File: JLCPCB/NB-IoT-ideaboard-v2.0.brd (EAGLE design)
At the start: 93 x 65 mm, 118 parts, among them Q1 32.768kHz, Q2 9013, Q3 9013, Q4 9013, Q5 9013, U1 STM32F103RBT6, U2 MCP73831T-2ACI/OT, U3 AP2112-3.3, U4 PAM2401, U5 MICROSIM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

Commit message: Readme.md
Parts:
- moved S4 0.20 mm to (30.7, 57.5)
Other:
- board text added: "BRAND"
- board text added: "Dialog IoT Device Information"
- board text added: "MAC"
- board text added: "MSISDN"
- board text added: "TYPE"
- board text added: "VERSION"

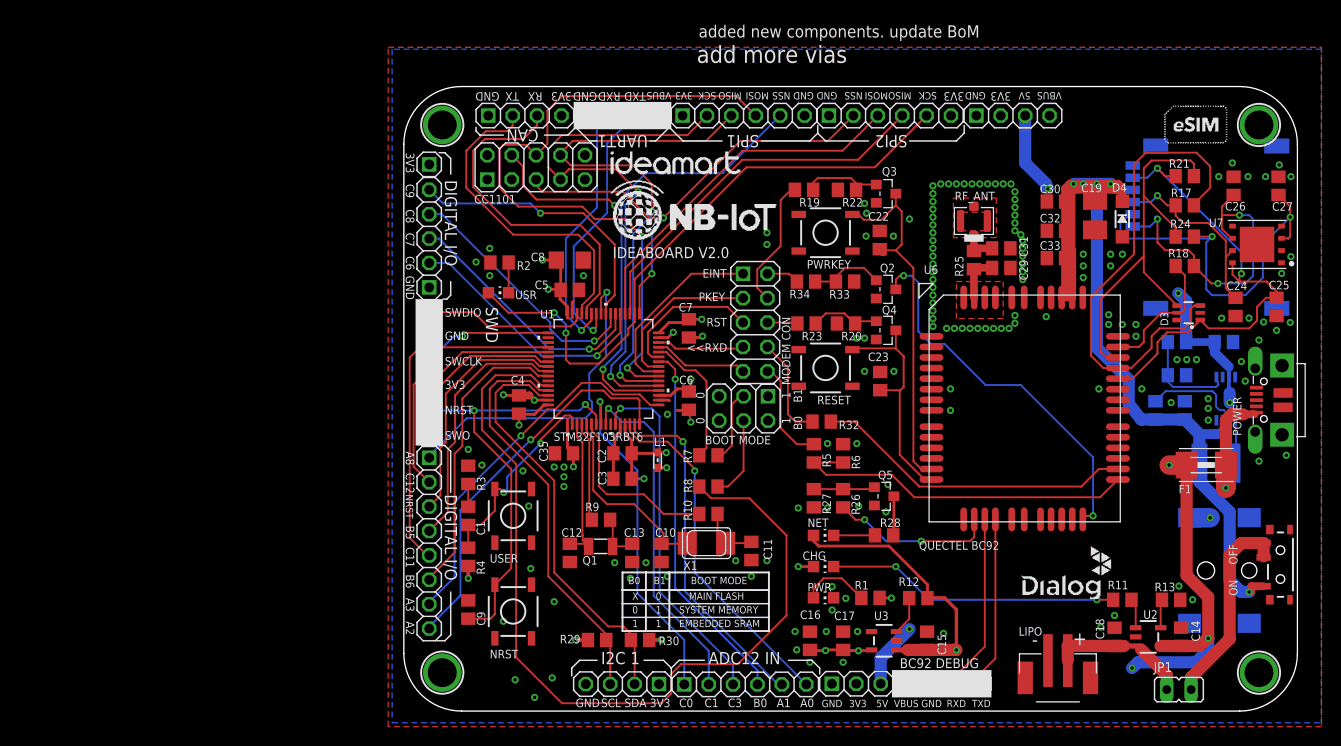
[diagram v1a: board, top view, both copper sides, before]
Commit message: Adds USB FS data lines for CDC Virtual Com port
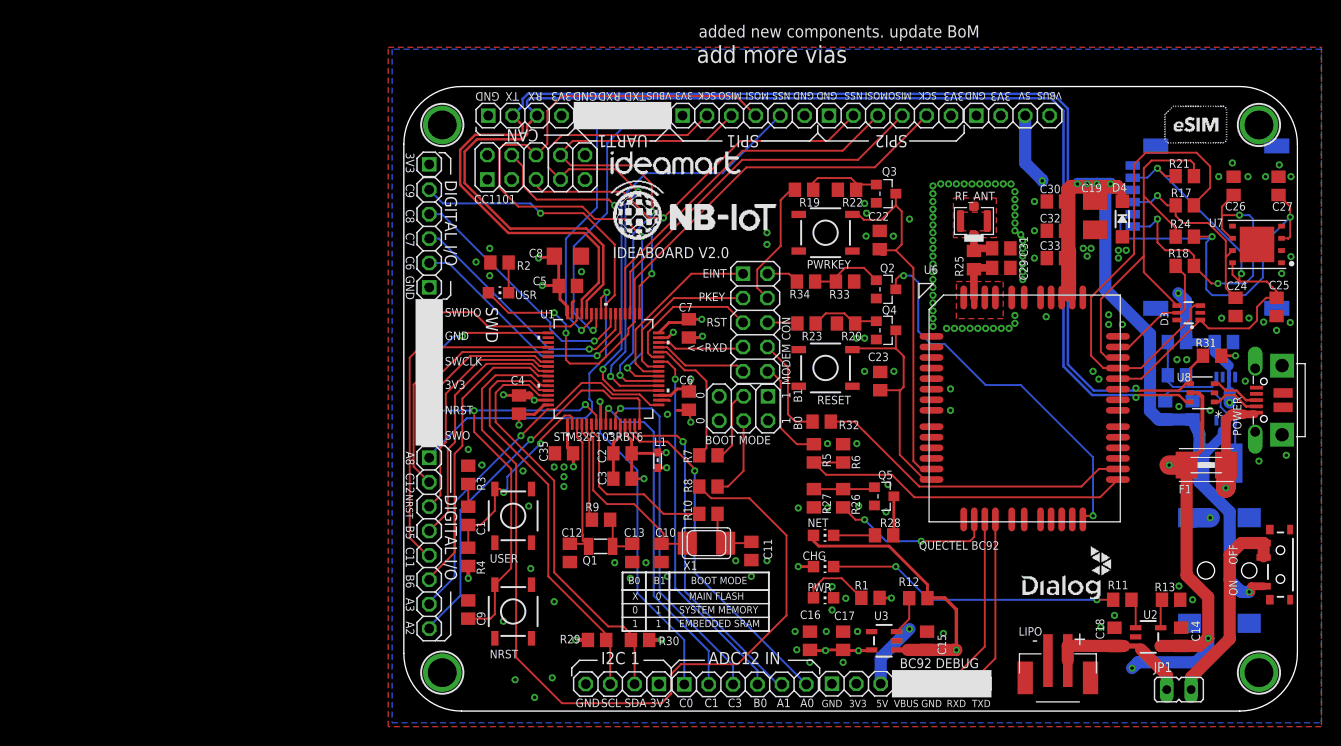
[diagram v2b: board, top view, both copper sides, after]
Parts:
- added R31: 1k5, rcl:R0805
- added U8: USBLC6-2SC6YSOT23-6L_STM-L, USBLC6:SOT23-6L_STM-L
- moved R14 1.02 mm to (98.6, 68.5)
- moved C20 0.81 mm to (101.4, 68.5)
- moved C5 0.45 mm to (36.4, 81.4)
- moved C8 0.45 mm to (36.4, 84.5)
- moved L2 0.20 mm to (104.0, 63.0)
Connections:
- removed net CAN_RX: CAN.3, U1.44
- removed net CAN_TX: CAN.2, U1.45
- removed net VSS: C2.1, C3.1, U1.12
- new net USB_CONN_D_N: POWER.D-, U8.1
- new net USB_CONN_D_P: POWER.D+, U8.3
- new net USB_D_N: CAN.3, U1.44, U8.6
- new net USB_D_P: CAN.2, R31.2, U1.45, U8.4
- net +3V3: now also R31.1
- net GND: now also C2.1, C3.1, U1.12, U8.2
- net VBUS: now also U8.5
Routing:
- net USB_D_P: track 0.00 -> 142.0 mm, vias 0 -> 1
- net USB_D_N: track 0.00 -> 137.8 mm, vias 0 -> 1
- net CAN_RX: track 36.1 -> 0.00 mm
- net CAN_TX: track 34.0 -> 0.00 mm
- net VBUS: track 193.5 -> 202.7 mm
- net GND: track 13.7 -> 19.9 mm, vias 154 -> 150
- net VSS: track 5.98 -> 0.00 mm
- net USB_CONN_D_N: track 0.00 -> 5.15 mm
- net USB_CONN_D_P: track 0.00 -> 5.07 mm
- net +3V3: track 42.1 -> 44.9 mm, vias 16 -> 17
- net SIM1_VDD: track 51.1 -> 49.5 mm
- net SIM1_RST: track 51.7 -> 50.7 mm
- net SIM1_CLK: track 14.2 -> 13.5 mm
- net V+: track 167.6 -> 166.9 mm
